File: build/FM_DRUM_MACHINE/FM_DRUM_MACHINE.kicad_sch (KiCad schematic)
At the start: 279 parts, among them J1 PJ-102A, J2 KICK_BUFFEREDOUT, J3 SNARE_BUFFEREDOUT, J4 HATS_BUFFEREDOUT, J5 TOMS_BUFFEREDOUT, J6 LINE_OUT, Q1 BC547, Q2 BC557, SW1 STEP1, SW10 STEP10, SW11 STEP11, SW12 STEP12, SW13 STEP13, SW14 STEP14, SW15 STEP15, SW16 STEP16, SW17 KICK_TRIG, SW18 SNARE_TRIG, SW19 CHAT_TRIG, SW2 STEP2, SW20 OHAT_TRIG, SW21 LOTOM_TRIG, SW22 HITOM_TRIG, SW23 PLAY/PAUSE, SW24 RECORD, SW25 SELECT, SW26 SW_DPDT_x2, SW27 SW_DPDT_x2, SW3 STEP3, SW4 STEP4, SW5 STEP5, SW6 STEP6, SW7 STEP7, SW8 STEP8, SW9 STEP9, U1 6N138, U10 TL074, U11 TL074, U13 TL074, U14 TL074, U2 TL072, U3 TL072, U4 TL074, U5 MAX7221xNG, U6 CD74HC4067M, U7 CD74HC4067M, U8 AMS1117-5.0, U9 AMS1117-3.3

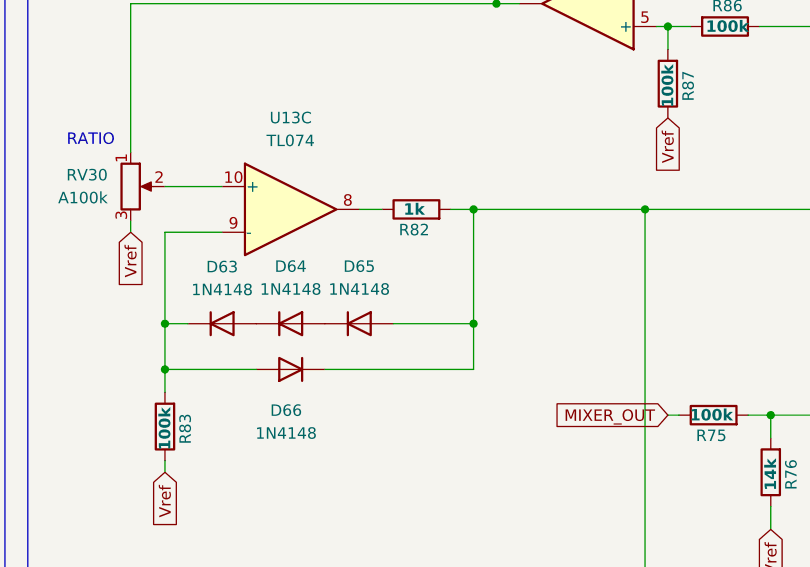
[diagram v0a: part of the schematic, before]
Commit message: LT_SPICE SImulations
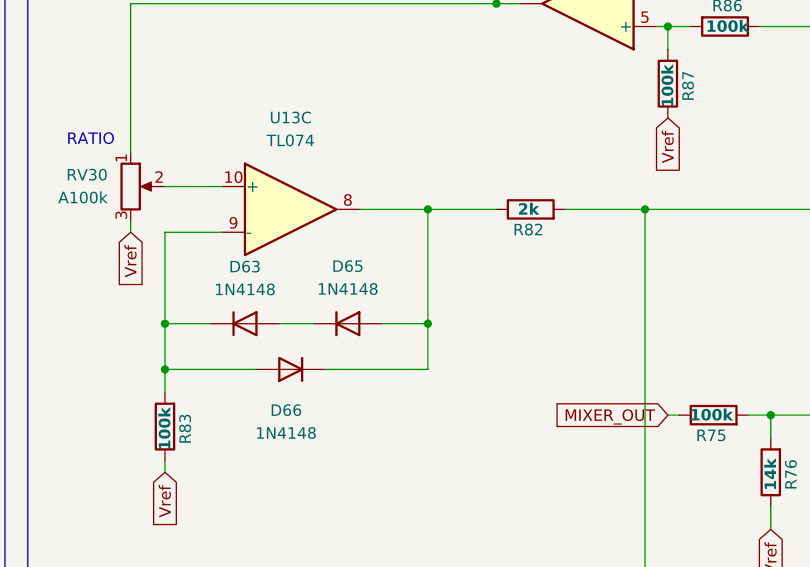
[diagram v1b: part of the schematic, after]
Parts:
- removed D64: 1N4148, PCM_4ms_Diode:D_DO-35_P7.62mm_Horizontal, symbol Diode:1N4148
- R82: value 1k -> 2k
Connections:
- net at D59.2 (A), R81.1, R82.2: no longer D65.2 (A), D66.1 (K)
- net at D63.2 (A): now also D65.1 (K)
- net at R82.1, U13.8: now also D65.2 (A), D66.1 (K)
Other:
- moved on the sheet: D63, D65, R82
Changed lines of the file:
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@@
 	)
 	(junction
-		(at 635 266.7)
-		(diameter 0)
-		(color 0 0 0 0)
-	)
-	(junction
 		(at 626.11 372.11)
 		(diameter 0)
@@
 	)
 	(junction
+		(at 610.87 266.7)
+		(diameter 0)
+		(color 0 0 0 0)
+	)
+	(junction
 		(at 648.97 289.56)
 		(diameter 0)
@@
 	)
 	(junction
-		(at 615.95 279.4)
-		(diameter 0)
-		(color 0 0 0 0)
-	)
-	(junction
 		(at 698.5 76.2)
 		(diameter 0)
@@
 	)
 	(junction
-		(at 247.65 584.2)
+		(at 610.87 279.4)
 		(diameter 0)
 		(color 0 0 0 0)
 	)
 	(junction
-		(at 262.89 313.69)
+		(at 247.65 584.2)
 		(diameter 0)
 		(color 0 0 0 0)
 	)
 	(junction
-		(at 615.95 266.7)
+		(at 262.89 313.69)
 		(diameter 0)
 		(color 0 0 0 0)
@@
 	)
 	(junction
+		(at 635 266.7)
+		(diameter 0)
+		(color 0 0 0 0)
+	)
+	(junction
 		(at 843.28 52.07)
 		(diameter 0)
@@
 	(wire
 		(pts
-			(xy 607.06 279.4) (xy 615.95 279.4)
+			(xy 605.79 279.4) (xy 610.87 279.4)
 		)
 		(stroke
@@
 	(wire
 		(pts
+			(xy 626.11 266.7) (xy 635 266.7)
+		)
+		(stroke
+			(width 0)
+			(type default)
+		)
+	)
+	(wire
+		(pts
 			(xy 247.65 254) (xy 250.19 254)
 		)
@@
 	(wire
 		(pts
-			(xy 581.66 279.4) (xy 584.2 279.4)
+			(xy 581.66 279.4) (xy 586.74 279.4)
 		)
 		(stroke
@@
 	(wire
 		(pts
-			(xy 599.44 284.48) (xy 615.95 284.48)
+			(xy 599.44 284.48) (xy 610.87 284.48)
 		)
 		(stroke
@@
 	(wire
 		(pts
-			(xy 613.41 266.7) (xy 615.95 266.7)
-		)
-		(stroke
-			(width 0)
-			(type default)
-		)
-	)
-	(wire
-		(pts
 			(xy 365.76 176.53) (xy 368.3 176.53)
 		)
@@
 	(wire
 		(pts
-			(xy 603.25 266.7) (xy 605.79 266.7)
+			(xy 603.25 266.7) (xy 610.87 266.7)
 		)
 		(stroke
@@
 	(wire
 		(pts
-			(xy 615.95 266.7) (xy 635 266.7)
-		)
-		(stroke
-			(width 0)
-			(type default)
-		)
-	)
-	(wire
-		(pts
 			(xy 457.2 495.3) (xy 457.2 497.84)
 		)
@@
 	(wire
 		(pts
-			(xy 615.95 279.4) (xy 615.95 266.7)
+			(xy 610.87 279.4) (xy 610.87 284.48)
 		)
 		(stroke
@@
 	(wire
 		(pts
+			(xy 610.87 266.7) (xy 610.87 279.4)
+		)
+		(stroke
+			(width 0)
+			(type default)
+		)
+	)
+	(wire
+		(pts
 			(xy 252.73 571.5) (xy 252.73 561.34)
 		)
@@
 	(wire
 		(pts
-			(xy 615.95 284.48) (xy 615.95 279.4)
-		)
-		(stroke
-			(width 0)
-			(type default)
-		)
-	)
-	(wire
-		(pts
 			(xy 254 313.69) (xy 254 312.42)
 		)
@@
 	(wire
 		(pts
+			(xy 610.87 266.7) (xy 618.49 266.7)
+		)
+		(stroke
+			(width 0)
+			(type default)
+		)
+	)
+	(wire
+		(pts
 			(xy 508 497.84) (xy 508 495.3)
 		)
@@
 	(wire
 		(pts
+			(xy 594.36 279.4) (xy 598.17 279.4)
+		)
+		(stroke
+			(width 0)
+			(type default)
+		)
+	)
+	(wire
+		(pts
 			(xy 255.27 162.56) (xy 254 162.56)
 		)
@@
 	(symbol
 		(lib_id "Diode:1N4148")
-		(at 588.01 279.4 0)
+		(at 590.55 279.4 0)
 		(unit 1)
 		(exclude_from_sim no)
@@
 		(fields_autoplaced yes)
 		(property "Reference" "D63"
-			(at 588.01 273.0996 0)
+			(at 590.55 273.0996 0)
 			(effects
 				(font
@@
 		)
 		(property "Value" "1N4148"
-			(at 588.01 275.6396 0)
+			(at 590.55 275.6396 0)
 			(effects
 				(font
@@
 		)
 		(property "Footprint" "PCM_4ms_Diode:D_DO-35_P7.62mm_Horizontal"
-			(at 588.01 279.4 0)
+			(at 590.55 279.4 0)
 			(effects
 				(font
@@
 		)
 		(property "Datasheet" "https://assets.nexperia.com/documents/data-sheet/1N4148_1N4448.pdf"
-			(at 588.01 279.4 0)
+			(at 590.55 279.4 0)
 			(effects
 				(font
@@
 		)
 		(property "Description" "100V 0.15A standard switching diode, DO-35"
-			(at 588.01 279.4 0)
+			(at 590.55 279.4 0)
 			(effects
 				(font
@@
 		)
 		(property "Sim.Device" "D"
-			(at 588.01 279.4 0)
+			(at 590.55 279.4 0)
 			(effects
 				(font
@@
 		)
 		(property "Sim.Pins" "1=K 2=A"
-			(at 588.01 279.4 0)
+			(at 590.55 279.4 0)
 			(effects
 				(font
@@
 	(symbol
 		(lib_id "Diode:1N4148")
-		(at 603.25 279.4 0)
+		(at 601.98 279.4 0)
 		(unit 1)
 		(exclude_from_sim no)
@@
 		(fields_autoplaced yes)
 		(property "Reference" "D65"
-			(at 603.25 273.05 0)
+			(at 601.98 273.05 0)
 			(effects
 				(font
@@
 		)
 		(property "Value" "1N4148"
-			(at 603.25 275.59 0)
+			(at 601.98 275.59 0)
 			(effects
 				(font
@@
 		)
 		(property "Footprint" "PCM_4ms_Diode:D_DO-35_P7.62mm_Horizontal"
-			(at 603.25 279.4 0)
+			(at 601.98 279.4 0)
 			(effects
 				(font
@@
 		)
 		(property "Datasheet" "https://assets.nexperia.com/documents/data-sheet/1N4148_1N4448.pdf"
-			(at 603.25 279.4 0)
+			(at 601.98 279.4 0)
 			(effects
 				(font
@@
 		)
 		(property "Description" "100V 0.15A standard switching diode, DO-35"
-			(at 603.25 279.4 0)
+			(at 601.98 279.4 0)
 			(effects
 				(font
@@
 		)
 		(property "Sim.Device" "D"
-			(at 603.25 279.4 0)
+			(at 601.98 279.4 0)
 			(effects
 				(font
@@
 		)
 		(property "Sim.Pins" "1=K 2=A"
-			(at 603.25 279.4 0)
+			(at 601.98 279.4 0)
 			(effects
 				(font
@@
 	(symbol
 		(lib_id "Device:R")
-		(at 609.6 266.7 90)
+		(at 622.3 266.7 90)
 		(unit 1)
 		(exclude_from_sim no)
@@
 		(dnp no)
 		(property "Reference" "R82"
-			(at 609.346 268.986 90)
+			(at 622.046 268.986 90)
 			(effects
 				(font
@@
 			)
 		)
-		(property "Value" "1k"
-			(at 609.346 266.7 90)
+		(property "Value" "2k"
+			(at 622.046 266.7 90)
 			(effects
 				(font
@@
 		)
 		(property "Footprint" "PCM_4ms_Resistor:R_Axial_DIN0207_L6.3mm_D2.5mm_P7.62mm_Horizontal"
-			(at 609.6 268.478 90)
+			(at 622.3 268.478 90)
 			(effects
 				(font
@@
 		)
 		(property "Datasheet" "~"
-			(at 609.6 266.7 0)
+			(at 622.3 266.7 0)
 			(effects
 				(font
@@
 		)
 		(property "Description" "Resistor"
-			(at 609.6 266.7 0)
+			(at 622.3 266.7 0)
 			(effects
 				(font
@@
 					(unit 1)
 				)
-			)
-		)
-	)
-	(symbol
-		(lib_id "Diode:1N4148")
-		(at 595.63 279.4 0)
-		(unit 1)
-		(exclude_from_sim no)
-		(in_bom yes)
-		(on_board yes)
-		(dnp no)
-		(fields_autoplaced yes)
-		(property "Reference" "D64"
-			(at 595.63 273.05 0)
-			(effects
-				(font
-					(size 1.27 1.27)
-				)
-			)
-		)
-		(property "Value" "1N4148"
-			(at 595.63 275.59 0)
-			(effects
-				(font
-					(size 1.27 1.27)
-				)
-			)
-		)
-		(property "Footprint" "PCM_4ms_Diode:D_DO-35_P7.62mm_Horizontal"
-			(at 595.63 279.4 0)
-			(effects
-				(font
-					(size 1.27 1.27)
-				)
-				(hide yes)
-			)
-		)
-		(property "Datasheet" "https://assets.nexperia.com/documents/data-sheet/1N4148_1N4448.pdf"
-			(at 595.63 279.4 0)
-			(effects
-				(font
-					(size 1.27 1.27)
-				)
-				(hide yes)
-			)
-		)
-		(property "Description" "100V 0.15A standard switching diode, DO-35"
-			(at 595.63 279.4 0)
-			(effects
-				(font
-					(size 1.27 1.27)
-				)
-				(hide yes)
-			)
-		)
-		(property "Sim.Device" "D"
-			(at 595.63 279.4 0)
-			(effects
-				(font
-					(size 1.27 1.27)
-				)
-				(hide yes)
-			)
-		)
-		(property "Sim.Pins" "1=K 2=A"
-			(at 595.63 279.4 0)
-			(effects
-				(font
-					(size 1.27 1.27)
-				)
-				(hide yes)
-			)
-		)
-		(pin "1"
-		)
-		(pin "2"
-		)
-		(instances
-			(project "FM_DRUM_MACHINE"
-				(path "/11c50643-64f9-4549-afde-9664eced946d"
-					(reference "D64")
-					(unit 1)
-				)

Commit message: Schematic PCB Changes
- Updated Power In
- Updated PCB
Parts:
- removed C7: 100uF, Capacitor_THT:CP_Radial_D5.0mm_P2.00mm, symbol Device:C_Polarized_US
- removed Q1: BC547, Package_TO_SOT_THT:TO-92L_Inline, symbol Transistor_BJT:BC547
- removed Q2: BC557, Package_TO_SOT_THT:TO-92_Inline, symbol Transistor_BJT:BC557
- removed R16: 10R, PCM_4ms_Resistor:R_Axial_DIN0207_L6.3mm_D2.5mm_P7.62mm_Horizontal, symbol Device:R
- removed R72: 1k, PCM_4ms_Resistor:R_Axial_DIN0207_L6.3mm_D2.5mm_P7.62mm_Horizontal, symbol Device:R
- removed R96, R97, R98, R99: 220R, PCM_4ms_Resistor:R_Axial_DIN0207_L6.3mm_D2.5mm_P7.62mm_Horizontal, symbol Device:R
- removed U3: TL072, Package_DIP:DIP-8_W7.62mm_LongPads, symbol PCM_4ms_IC:TL072
- added U12, U3: OPA551P, Package_DIP:DIP-8_W7.62mm, symbol Amplifier_Operational:OPA551P
- D10, D11, D12, D13, D14, D15, D16, D17, D18, D19, D20, D21, D22, D23, D24, D25, D26, D27, D28, D29, D5, D6, D7, D8, D9: value Random Diode -> 1N4148
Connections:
- net A12V is gone; now on net 12V: C1.1, R70.1, R88.1, U10.4 (V+), U11.4 (V+), U13.4 (V+), U14.4 (V+), U2.8 (V+), U4.4 (V+)
- net 12V: now also U12.7 (V+), U3.7 (V+)
- net AGND: no longer J2.S, J3.S, J4.S, J5.S, J6.S, RV33.1, RV35.1, RV39.1, RV40.1, RV46.1, U10.11 (V-), U11.11 (V-), U13.11 (V-), U14.11 (V-), U2.4 (V-), U4.11 (V-)
- net DGND: now also J2.S, J3.S, J4.S, J5.S, J6.S, RV33.1, RV35.1, RV39.1, RV40.1, RV46.1, U10.11 (V-), U11.11 (V-), U13.11 (V-), U14.11 (V-), U2.4 (V-), U4.11 (V-), U12.4 (V-), U12.8 (Flag), U3.4 (V-), U3.8 (Flag); no longer R7.1
- net Vref: now also U12.2 (-), U12.6
- net at TRS_JACK_1.R, TRS_JACK_2.R: now also R7.2; no longer D1.2 (A), U1.3 (C2)
- net at TRS_JACK_1.T, TRS_JACK_2.T: now also D1.2 (A), U1.3 (C2)
- net at C1.2, C2.1: now also U12.3 (+), U3.2 (-), U3.6
- net at D1.1 (K), U1.2 (C1): now also R7.1; no longer R7.2
- net at C73.2, R70.2, R71.1: now also U3.3 (+)
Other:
- moved on the sheet: C1, C2, C69, C70, C71, C72, C73, D3, D4, D54, J1, R51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
